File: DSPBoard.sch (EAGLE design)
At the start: 384 parts, among them IC1 AD1939WBSTZ, IC10 LM833D, IC11 LM833D, IC12 TL074D, IC13 CD74HC4094M96, IC14 CD74HC4094M96, IC2 25AA1024-I_SM, IC3 LM4040B10DBZ, IC4 LM833D, IC5 LM833D, IC6 LM833D, IC7 LM833D, IC8 LM833D, IC9 LM833D, U1 LM11173.3NOPB, U2 PEC11R-4315F-N0012, U3 PEC11R-4315F-N0012, X1 2510-, Y1 12.288MHz

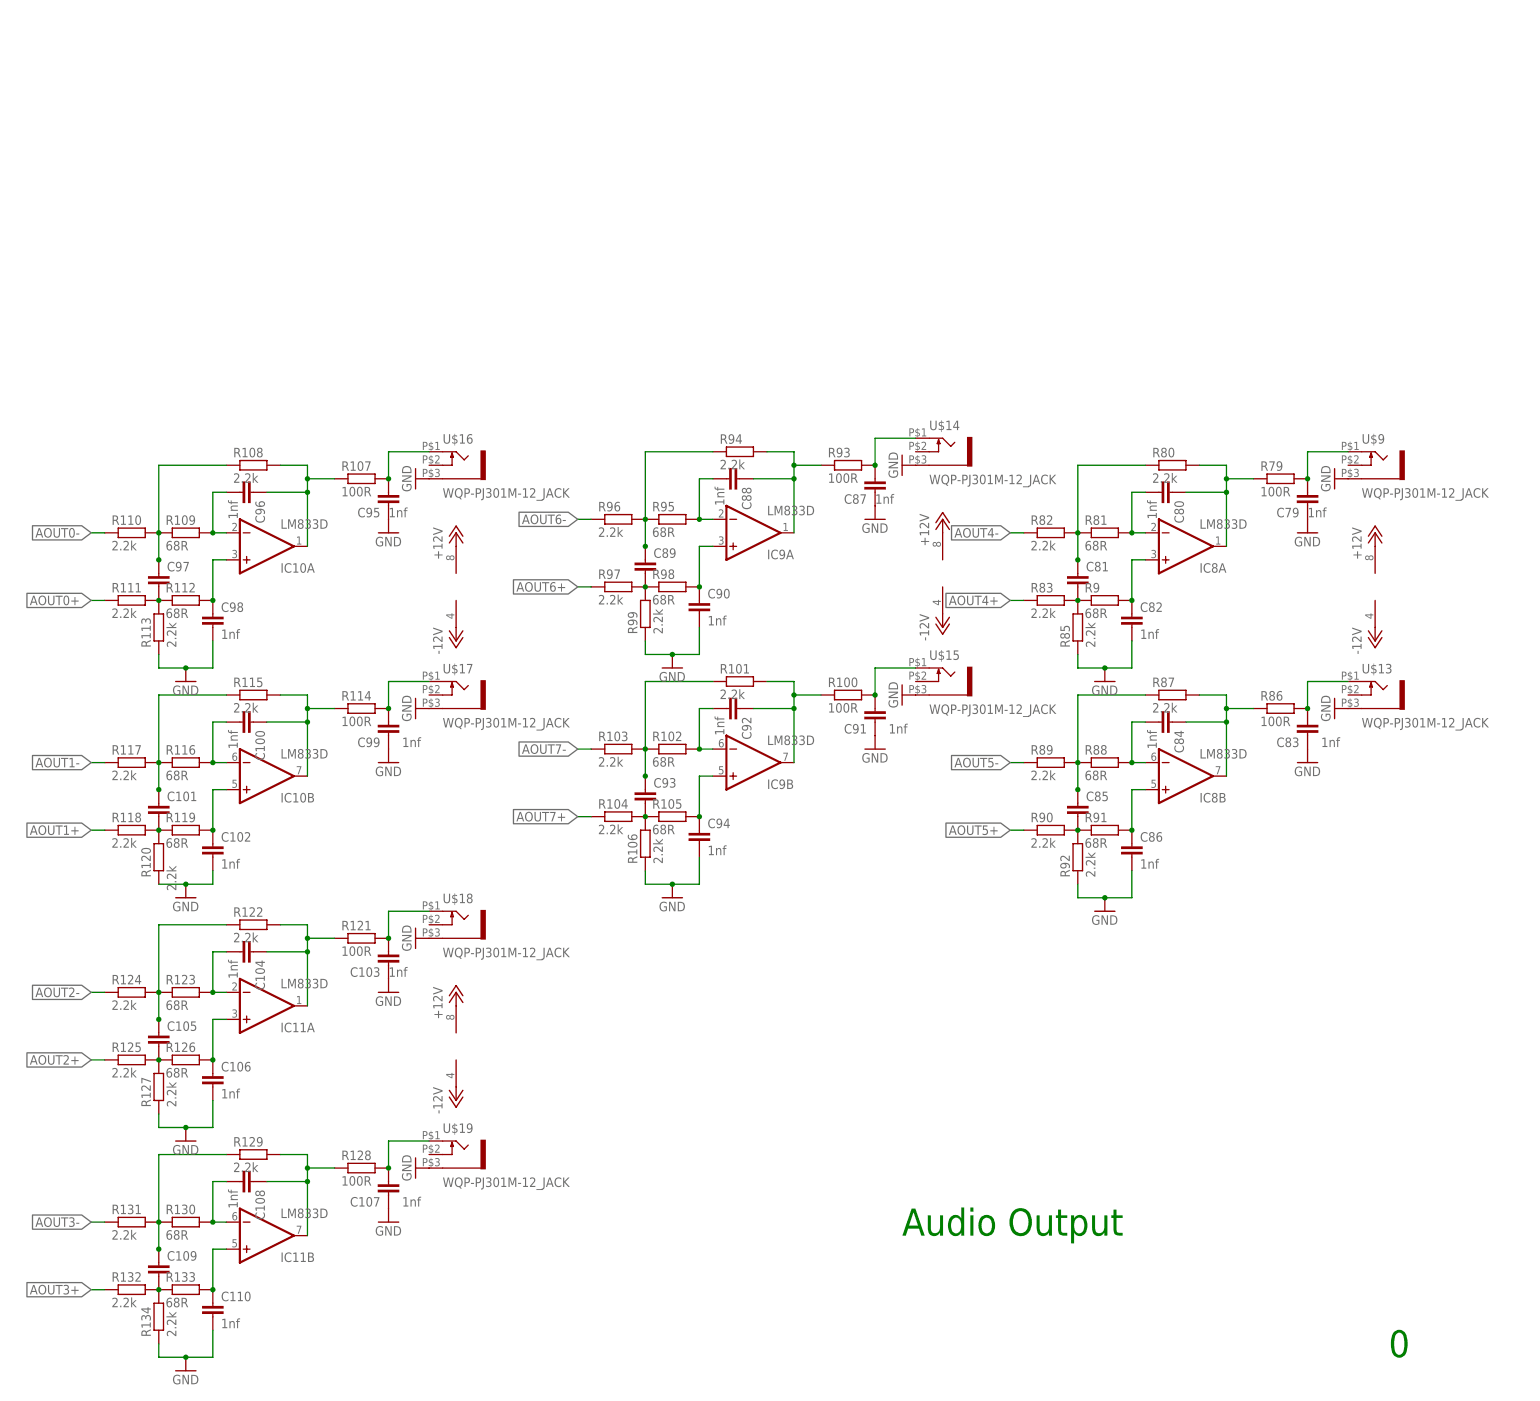
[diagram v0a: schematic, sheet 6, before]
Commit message: tidied analog outputs and tactile controls
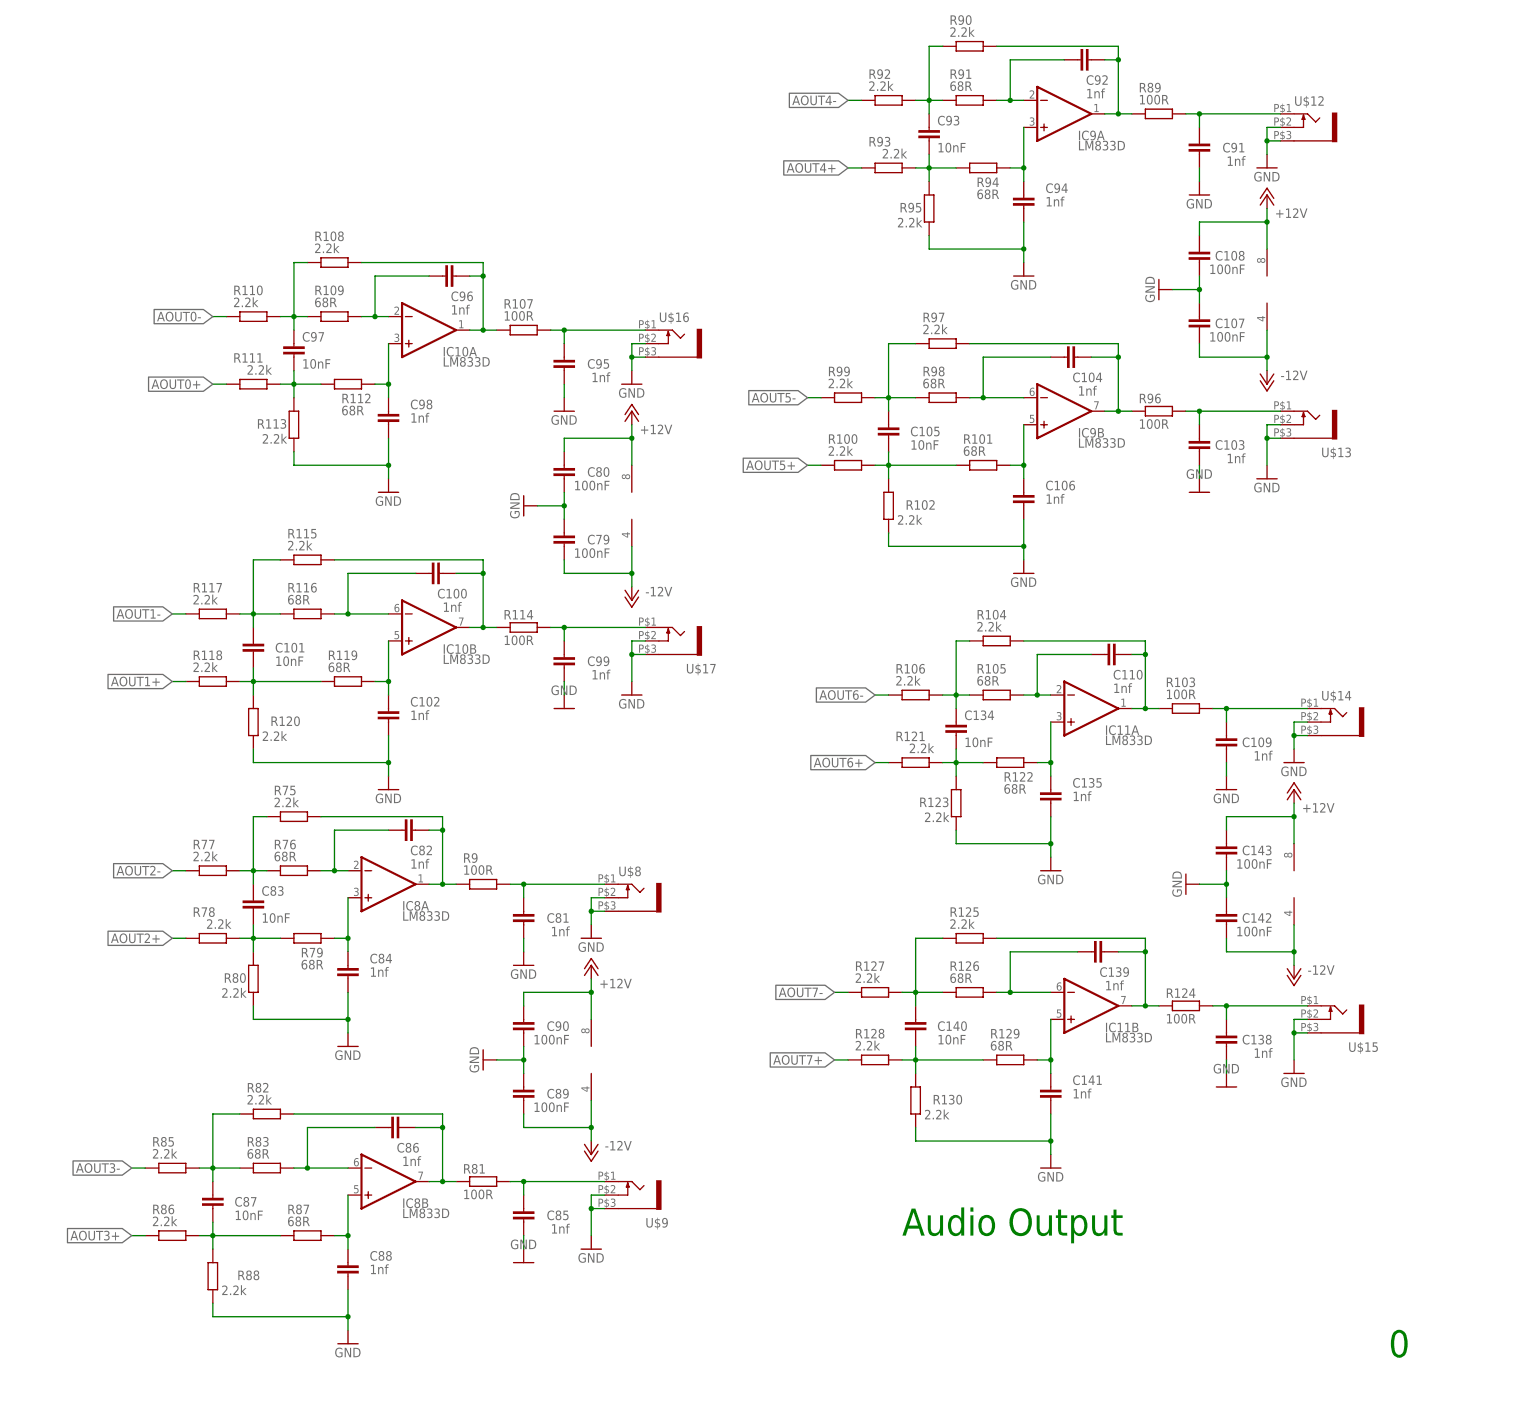
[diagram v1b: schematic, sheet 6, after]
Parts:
- removed R131, R132, R134: 2.2k, rcl:R-EU_R0805
- removed R133: 68R, rcl:R-EU_R0805
- removed U$18, U$19: WQP-PJ301M-12_JACK, thonkiconn:WQP-PJ301M-12_JACK
- added C138, C139, C141: 1nf, rcl:C-EUC0805
- added C140: 10nF, rcl:C-EUC0805
- added C142, C143: 100nF, rcl:C-EUC0805
- added C17, C25: 100nf, rcl:C-EUC0805
- added R15: 15k, rcl:R-EU_R0805
- added R30: 2.7k, rcl:R-EU_R0805
- added R32, R54: 2.2k, rcl:R-EU_R0805
- added U$12, U$8: WQP-PJ301M-12_JACK, thonkiconn:WQP-PJ301M-12_JACK
- C101, C105, C93, C97: value (none) -> 10nF
- C107, C108, C79, C80, C90: value 1nf -> 100nF
- C109, C81, C85: value (none) -> 1nf
- C134: value 100pF -> 10nF
- C135: value 10nF -> 1nf
- C50, C61, C72: value 100nf -> 220uF; device rcl:C-EUC0805 -> rcl:CPOL-EU140CLH-1014
- C51, C62, C73: value 100nf -> 1nF
- C52, C63, C74: value 220uF -> 470p; device rcl:CPOL-EU140CLH-1014 -> rcl:C-EUC0805
- C53, C64, C75: value 1nF -> 1uF
- C54, C65, C76: value 470p -> 100uF; device rcl:C-EUC0805 -> rcl:CPOL-EU140CLH-0810
- C55, C66, C77: value 1uF -> 100pF
- C56, C67, C78: value 100uF -> 10nF; device rcl:CPOL-EU140CLH-0810 -> rcl:C-EUC0805
- C59, C70: value 100pF -> 100nf
- C60, C71: value 10nF -> 100nf
- C83, C87: value 1nf -> 10nF
- C89: value (none) -> 100nF
- R100, R121, R128, R86, R93: value 100R -> 2.2k
- R101, R122, R129, R83, R87, R94: value 2.2k -> 68R
- R102, R123, R130, R88, R95: value 68R -> 2.2k
- R103, R124, R89, R96: value 2.2k -> 100R
- R34: value (none) -> 2.2k
- R42: value 15k -> 2.2k
- R43: value 2.7k -> 12.7k
- R44, R61, R71: value (none) -> 10k
- R45, R62, R72: value 2.2k -> 10k
- R46: value 12.7k -> 10k
- R47, R48, R64, R74: value 10k -> 22R
- R49, R65: value 10k -> 15k
- R50: value 22R -> 2.7k
- R51, R67, R68, R77, R78: value 22R -> 2.2k
- R55, R69: value 15k -> 12.7k
- R57, R70: value 2.7k -> 10k
- R63, R73: value 12.7k -> 22R
- R66: value 10k -> 2.7k
- R75: value 10k -> 2.2k
- R76: value 10k -> 68R
- R79: value 100R -> 68R
- R81, R9: value 68R -> 100R
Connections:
- removed net N$108: C105.1, R122.1, R123.1, R124.2
- removed net N$109: C105.2, R125.2, R126.1, R127.2
- removed net N$110: C106.1, IC11A.+IN, R126.2
- removed net N$111: C107.2, R128.2, U$19.2
- removed net N$112: C108.1, IC11B.OUT, R128.1, R129.2
- removed net N$113: C108.2, IC11B.-IN, R130.2
- removed net N$114: C109.1, R129.1, R130.1, R131.2
- removed net N$115: C109.2, R132.2, R133.1, R134.2
- removed net N$116: C110.1, IC11B.+IN, R133.2
- removed net N$121: C81.2, R83.2, R85.2, R9.1
- removed net N$17 (its old number): C79.2, R79.2, U$9.2
- removed net N$22 (its old number): C80.1, IC8A.OUT, R79.1, R80.2
- removed net N$59 (its old number): C76.2, IC7A.+IN, R70.2
- removed net N$60 (its old number): C75.2, IC7A.-IN, IC7A.OUT, R71.2, R78.2
- removed net N$61 (its old number): IC7B.-IN, R71.1, R72.2
- removed net N$62 (its old number): IC7B.OUT, R72.1, R77.2
- removed net N$63 (its old number): C77.2, IC7B.+IN, R73.1
- removed net N$64 (its old number): C77.1, C78.+, R73.2, R74.2, R75.1, R76.1
- removed net N$65 (its old number): C78.-, R74.1
- removed net N$66 (its old number): C132.1, C134.2
- removed net N$67 (its old number): C135.2, C74.-, U$7.2
- removed net N$68 (its old number): C135.1, C74.+, R69.1
- new net N$100: C141.1, IC11B.+IN, R129.2
- new net N$101: C138.2, R124.2, U$15.2
- new net N$102: C109.2, R103.2, U$14.2
- new net N$103: C110.1, IC11A.OUT, R103.1, R104.2
- new net N$104: C110.2, IC11A.-IN, R105.2
- new net N$40: C50.+, C58.1, R15.1
- new net N$41: C62.1, R49.2, R50.1, R62.2
- new net N$93: C93.1, R90.1, R91.1, R92.2
- new net N$94: C93.2, R93.2, R94.1, R95.2
- new net N$95: C94.1, IC9A.+IN, R94.2
- new net N$96: C139.2, IC11B.-IN, R126.2
- new net N$97: C140.1, R125.1, R126.1, R127.2
- new net N$98: C140.2, R128.2, R129.1, R130.2
- new net N$99: C139.1, IC11B.OUT, R124.1, R125.2
- net +12V: now also C108.2, C143.2, C17.1, C59.1, C70.1, C80.2, C90.2; no longer C50.1, C61.1, C72.1
- net -12V: now also C107.1, C142.1, C25.2, C60.2, C71.2, C79.1, C89.1; no longer C51.2, C62.2, C73.2
- net 3V3A: now also R45.2, R61.2, R71.2; no longer R48.2, R65.2, R75.2
- net AIN1+: now also C56.2, C57.1, R47.1; no longer C58.2, C59.1, R50.1
- net AIN1-: now also C55.2, C56.1, R48.1; no longer C57.2, C58.1, R51.1
- net AIN2+: now also C67.2, C68.1, R63.1; no longer C69.2, C70.1, R67.1
- net AIN2-: now also C66.2, C67.1, R64.1; no longer C68.2, C69.1, R68.1
- net AIN3+: now also C132.1, C78.2, R73.1; no longer C133.2, C134.1, R77.1
- net AIN3-: now also C77.2, C78.1, R74.1; no longer C132.2, C133.1, R78.1
- net AOUT2+: now also R78.1; no longer R125.1
- net AOUT2-: now also R77.1; no longer R124.1
- net AOUT3+: now also R86.1; no longer R132.1
- net AOUT3-: now also R85.1; no longer R131.1
- net AOUT4+: now also R93.1; no longer R83.1
- net AOUT4-: now also R92.1; no longer R82.1
- net AOUT5+: now also R100.1; no longer R90.1
- net AOUT5-: now also R99.1; no longer R89.1
- net AOUT6+: now also R121.1; no longer R97.1
- net AOUT6-: now also R106.1; no longer R96.1
- net AOUT7+: now also R128.1; no longer R104.1
- net AOUT7-: now also R127.1; no longer R103.1
- net GND: now also C107.2, C108.1, C109.1, C132.2, C135.2, C138.1, C141.2, C142.2, C143.1, C17.2, C25.1, C39.-, C46.1, C48.2, C52.1, C54.-, C55.1, C57.2, C59.2, C60.1, C63.1, C65.-, C66.1, C68.2, C70.2, C71.1, C74.1, C76.-, C77.1, C79.2, C80.1, C81.1, C84.2, C85.1, C88.2, C89.2, C90.1, R102.1, R123.1, R130.1, R37.1, R44.1, R57.1, R70.1, R80.1, R88.1, R95.1, U$12.1, U$12.3, U$13.3, U$14.3, U$15.3, U$16.3, U$17.3, U$8.1, U$8.3, U$9.3; no longer C107.1, C110.2, C50.2, C51.1, C54.1, C61.2, C62.1, C65.1, C72.2, C73.1, C76.1, C79.1, C82.2, C83.1, C86.2, C87.1, C90.2, R106.1, R127.1, R134.1, R85.1, R92.1, R99.1, U$18.1, U$19.1
- net N$105: now also C134.1, R104.1, R105.1, R106.2; no longer C103.2, R121.2, U$18.2
- net N$106: now also C134.2, R121.2, R122.1, R123.2; no longer C104.1, IC11A.OUT, R121.1, R122.2
- net N$107: now also C135.1, IC11A.+IN, R122.2; no longer C104.2, IC11A.-IN, R123.2
- net N$19: now also C51.1, R15.2, R30.1, R46.2; no longer C39.-, R37.1
- net N$20: now also C52.2, IC5A.+IN, R30.2; no longer C46.1, C48.2
- net N$23: now also C51.2, IC5A.-IN, IC5A.OUT, R32.2, R48.2; no longer C53.1, R42.2, R43.1, R49.2
- net N$25: now also IC5B.-IN, R32.1, R42.2; no longer C54.2, IC5A.+IN, R43.2
- net N$26: now also IC5B.OUT, R42.1, R47.2; no longer C53.2, IC5A.-IN, IC5A.OUT, R44.2, R51.2
- net N$34: now also C53.2, IC5B.+IN, R43.1; no longer IC5B.-IN, R44.1, R45.2
- net N$36: now also C53.1, C54.+, R43.2, R44.2, R46.1; no longer IC5B.OUT, R50.2
- net N$38: now also C50.-, C58.2, U$5.2; no longer C55.2, IC5B.+IN, R46.1
- net N$42: now also C63.2, IC6A.+IN, R50.2; no longer C55.1, C56.+, R46.2, R47.2, R48.1, R49.1
- net N$43: now also C62.2, IC6A.-IN, IC6A.OUT, R51.2, R64.2; no longer C56.-, R47.1
- net N$44: now also IC6B.-IN, R51.1, R54.2; no longer C57.1, C59.2
- net N$45: now also IC6B.OUT, R54.1, R63.2; no longer C52.-, C60.2, U$5.2
- net N$46: now also C64.2, IC6B.+IN, R55.1; no longer C52.+, C60.1, R42.1
- net N$47: now also C65.+, R57.2, R61.1, R62.1; no longer R57.1, R66.2
- net N$48: now also C61.-, C69.2, U$6.2; no longer C65.2, IC6A.+IN, R57.2
- net N$49: now also C61.+, C69.1, R49.1; no longer C64.2, IC6A.-IN, IC6A.OUT, R61.2, R68.2
- net N$50: now also C73.1, R65.2, R66.1, R72.2; no longer IC6B.-IN, R61.1, R62.2
- net N$51: now also C74.2, IC7A.+IN, R66.2; no longer IC6B.OUT, R62.1, R67.2
- net N$52: now also C73.2, IC7A.-IN, IC7A.OUT, R67.2, R74.2; no longer C66.2, IC6B.+IN, R63.1
- net N$53: now also IC7B.-IN, R67.1, R68.2; no longer C66.1, C67.+, R63.2, R64.2, R65.1, R66.1
- net N$54: now also IC7B.OUT, R68.1, R73.2; no longer C67.-, R64.1
- net N$55: now also C75.2, IC7B.+IN, R69.1; no longer C68.1, C70.2
- net N$56: now also C75.1, C76.+, R69.2, R70.2, R71.1, R72.1; no longer C63.-, C71.2, U$6.2
- net N$57: now also C133.2, C72.-, U$7.2; no longer C63.+, C71.1, R55.1
- net N$58: now also C133.1, C72.+, R65.1; no longer C75.1, R69.2, R70.1, R76.2
- net N$70: now also C86.2, IC8B.-IN, R83.2; no longer C80.2, IC8A.-IN, R81.2
- net N$71: now also C87.1, R82.1, R83.1, R85.2; no longer C81.1, R80.1, R81.1, R82.2
- net N$72: now also C87.2, R86.2, R87.1, R88.2; no longer C82.1, IC8A.+IN, R9.2
- net N$73: now also C86.1, IC8B.OUT, R81.1, R82.2; no longer C83.2, R86.2, U$13.2
- net N$74: now also C88.1, IC8B.+IN; no longer C84.1, IC8B.OUT, R86.1
- net N$77: now also C85.2, R81.2, U$9.2; no longer C84.2, IC8B.-IN, R88.2
- net N$78: now also C81.2, R9.2, U$8.2; no longer C85.1, R87.1, R88.1, R89.2
- net N$79: now also C82.1, IC8A.OUT, R75.2, R9.1; no longer C85.2, R90.2, R91.1, R92.2
- net N$80: now also C82.2, IC8A.-IN, R76.2; no longer C86.1, IC8B.+IN, R91.2
- net N$81: now also C83.1, R75.1, R76.1, R77.2; no longer C87.2, R93.2, U$14.2
- net N$82: now also C83.2, R78.2, R79.1, R80.2; no longer C88.1, IC9A.OUT, R93.1, R94.2
- net N$83: now also C84.1, IC8A.+IN, R79.2; no longer C88.2, IC9A.-IN, R95.2
- net N$84: now also C104.2, IC9B.-IN, R98.2; no longer C89.1, R94.1, R95.1, R96.2
- net N$85: now also C105.1, R97.1; no longer C89.2, R97.2
- net N$86: now also C105.2, R100.2, R101.1, R102.2; no longer C90.1, IC9A.+IN, R98.2
- net N$87: now also C104.1, IC9B.OUT, R96.1, R97.2; no longer C91.2, R100.2, U$15.2
- net N$88: now also C106.1, IC9B.+IN; no longer C92.1, IC9B.OUT, R100.1
- net N$89: now also C103.2, R96.2, U$13.2; no longer C92.2, IC9B.-IN, R102.2
- net N$90: now also C91.2, R89.2, U$12.2; no longer C93.1, R101.1, R102.1, R103.2
- net N$91: now also C92.1, IC9A.OUT, R89.1, R90.2; no longer C93.2, R104.2, R105.1, R106.2
- net N$92: now also C92.2, IC9A.-IN, R91.2; no longer C94.1, IC9B.+IN, R105.2
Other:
- moved on the sheet: C100, C101, C102, C103, C104, C105, C106, C107, C108, C109, C110, C132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

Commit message: just need to add cycling diodes to schematic and board
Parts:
- removed U$22, U$24: WQP-PJ301M-12_JACK, thonkiconn:WQP-PJ301M-12_JACK
- removed VR5: 10k, SparkFun-Resistors:POTENTIOMETER-PTH-9MM-1/20W-20%-KIT
- added C144, C145: 100nF, rcl:C-EUC0805
- added D1: BAV99,215, SamacSys_Parts:BAV99,215
- added IC17, IC18, LED_STROBE1: CD74HC4094M96, CD74HC4094M96:CD74HC4094M96
- added LED25, LED26, LED27, LED28, LED29, LED30, LED31, LED32, LED33, LED34, LED35, LED36, LED37, LED38, LED39, LED40, LED41, LED42, LED43, LED44, LED45, LED46, LED47, LED48: (no value), led:LEDCHIPLED_0805
- added R131, R132: 200k, rcl:R-EU_R0805
- added R133: 100k, rcl:R-EU_R0805
- added R134: 15k, rcl:R-EU_R0805
- added R154, R155, R156, R157, R158, R159, R160, R161, R163, R164, R189, R190, R195, R196, R197, R198, R199, R200, R201, R202: 470R, rcl:R-EU_R0805
- added R191, R192, R193, R194: 470, rcl:R-EU_R0805
- added U$18, U$19: WQP-PJ301M-12_JACK, thonkiconn:WQP-PJ301M-12_JACK
- added VR1: 100k, SparkFun-Resistors:POTENTIOMETER-PTH-9MM-1/20W-20%-KIT
- C124, C125, C126, C127: value (none) -> 10nF
- R136, R137, R138, R28: value (none) -> 10k
- R143, R149: value 33k -> 15k
- R144, R147, R150: value 200k -> 100k
- R146: value 33k -> 200k
- R151: value 100k -> 15k
- R152: value 33k -> 100k
- R165, R166, R167, R168, R169, R170, R171, R172, R173, R174, R175, R176, R181, R182, R183, R184, R185, R186, R187, R188: value (none) -> 470R
- R177, R178, R179, R180: value (none) -> 470
- VR2: value 10k -> 100k
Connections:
- removed net 1VREF: IC12A.+IN, IC12B.+IN, IC12C.+IN, IC12D.+IN
- removed net N$132 (its old number): C128.1, IC12A.-IN, R139.2, R143.2, R144.2
- removed net N$134 (its old number): R145.1, U$22.2
- removed net N$135 (its old number): R147.1, VR3.S
- removed net N$137 (its old number): C129.1, IC12B.-IN, R145.2, R146.2, R147.2
- new net LED_S3: IC17.DATA, IC18.QS1
- new net LED_S4: IC17.QS1, LED_STROBE1.DATA
- new net N$111: C128.1, IC12A.-IN, R131.2, R139.2, R143.2, R144.2
- new net N$113: C130.1, IC12C.-IN, R132.2, R148.2, R149.2, R150.2
- new net N$114: R145.1, VR1.S
- new net N$115: R133.1, U$18.2
- new net N$116: C129.1, IC12B.+IN, R133.2, R134.2, R145.2, R146.2
- new net N$118: R147.1, U$19.2
- new net N$121: R152.1, VR3.S
- new net N$122: C131.1, IC12D.+IN, R147.2, R151.2, R152.2, R153.2
- new net N$144: IC17.Q5, R155.1
- new net N$145: IC17.Q3, R158.2
- new net N$146: IC17.Q2, R159.2
- new net N$147: IC17.Q0, R161.2
- new net N$152: LED_STROBE1.Q4, R195.1
- new net N$153: LED_STROBE1.Q5, R196.1
- new net N$154: LED_STROBE1.Q6, R197.1
- new net N$155: LED_STROBE1.Q7, R198.1
- new net N$156: LED_STROBE1.Q3, R199.2
- new net N$157: LED_STROBE1.Q2, R200.2
- new net N$158: LED_STROBE1.Q1, R201.2
- new net N$159: LED_STROBE1.Q0, R202.2
- new net N$160: LED25.A, R154.2
- new net N$161: LED26.A, R155.2
- new net N$163: LED27.A, R156.2
- new net N$164: LED28.A, R157.2
- new net N$166: LED29.A, R158.1
- new net N$167: LED30.A, R159.1
- new net N$170: LED31.A, R160.1
- new net N$173: LED32.A, R161.1
- new net N$174: LED33.A, R163.1
- new net N$175: LED34.A, R164.1
- new net N$178: LED35.A, R189.1
- new net N$213: LED36.A, R190.1
- new net N$214: LED37.A, R191.2
- new net N$215: LED38.A, R192.2
- new net N$216: LED39.A, R193.2
- new net N$217: LED40.A, R194.2
- new net N$218: LED41.A, R195.2
- new net N$219: LED42.A, R196.2
- new net N$220: LED43.A, R197.2
- new net N$221: LED44.A, R198.2
- new net N$222: LED45.A, R199.1
- new net N$223: LED46.A, R200.1
- new net N$224: LED47.A, R201.1
- new net N$225: LED48.A, R202.1
- new net N$226: IC18.Q5, R193.1
- new net N$227: IC18.Q1, R164.2
- new net N$228: IC18.Q2, R189.2
- new net N$229: IC18.Q3, R190.2
- new net N$230: IC17.Q4, R154.1
- new net N$231: IC17.Q6, R156.1
- new net N$232: IC17.Q7, R157.1
- new net N$233: IC17.Q1, R160.2
- net +12V: now also C144.1
- net +3V3: now also IC17.OE, IC17.VCC, IC18.OE, IC18.VCC, LED_STROBE1.OE, LED_STROBE1.VCC
- net -10V: now also R131.1, R132.1, R146.1, R153.1, VR1.E; no longer VR5.E
- net -12V: now also C145.2
- net CV1: now also R134.1; no longer R146.1
- net CV3: now also R151.1; no longer R152.1
- net GND: now also C144.2, C145.1, IC12A.+IN, IC12B.-IN, IC12C.+IN, IC12D.-IN, IC17.GND, IC18.GND, LED25.C, LED26.C, LED27.C, LED28.C, LED29.C, LED30.C, LED31.C, LED32.C, LED33.C, LED34.C, LED35.C, LED36.C, LED37.C, LED38.C, LED39.C, LED40.C, LED41.C, LED42.C, LED43.C, LED44.C, LED45.C, LED46.C, LED47.C, LED48.C, LED_STROBE1.GND, U$18.1, U$18.3, U$19.1, U$19.3, VR1.A; no longer U$22.1, U$22.3, U$24.1, U$24.3, VR5.A
- net LED_CLK: now also IC18.CP, LED_STROBE1.CP
- net LED_DATA1: now also IC14.DATA, IC17.CP; no longer IC13.DATA
- net LED_DATA2: now also IC18.DATA
- net LED_S1: now also IC13.DATA, IC14.QS1; no longer IC13.QS1, IC14.DATA
- net LED_S2: now also IC13.QS1; no longer IC13.QS2
- net LED_STROBE: now also IC17.STROBE, IC18.STROBE, LED_STROBE1.STROBE
- net N$148: now also IC18.Q0, R163.2; no longer C130.1, IC12C.-IN, R148.2, R149.2, R150.2
- net N$149: now also IC18.Q7, R191.1; no longer R151.1, U$24.2
- net N$150: now also IC18.Q6, R192.1; no longer R153.1, VR5.S
- net N$151: now also IC18.Q4, R194.1; no longer C131.1, IC12D.-IN, R151.2, R152.2, R153.2
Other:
- note added: "0.1"
- note added: "LED Drivers"
- note added: "Tactile and CV Controls"
- note removed: "0"
- note removed: "User Control & LEDs"
